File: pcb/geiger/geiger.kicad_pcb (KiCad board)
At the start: 2 copper layers, 160 x 112.4 mm, 125 parts, among them J1 Conn_01x02, J2 Conn_01x02, J3 Conn_01x03, J4 Conn_01x06, J5 Conn_01x02, J6 Conn_02x05_Odd_Even, J7 Conn_02x05_Odd_Even, K1 RELAY_DPST, Q1 BC140, Q2 BC107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

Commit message: Final version of geiger board.
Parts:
- moved R39 1.59 mm to (80.3, 82.2)
- moved C9 1.59 mm to (34.3, 27.6)
- moved R6 0.95 mm to (43.5, 27.3)
- moved D2 0.71 mm to (40.6, 34.0)
- moved C31 0.45 mm to (24.1, 54.9)
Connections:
- J4 pad 5: (no net) -> GND
- V1 pad 3: GND -> HEATER_6_3V
- V1 pad 4: HEATER_6_3V -> GND
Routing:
- net GND: track 98.3 -> 117.8 mm
- net HEATER_6_3V: track 66.8 -> 56.3 mm
- net HEATER1: track 101.7 -> 96.3 mm
- net Net-(Q6-Pad2): track 99.8 -> 102.4 mm
- net HEATER2: track 73.5 -> 71.6 mm
- net Net-(C24-Pad2): track 37.5 -> 35.9 mm
- net EYE_GRID: track 73.9 -> 75.5 mm
- net -VDC: track 140.1 -> 141.0 mm
- net +5V: track 268.1 -> 268.8 mm
- net Net-(D6-Pad1): track 70.4 -> 71.0 mm
- net Net-(C8-Pad1): track 58.8 -> 59.5 mm
- net Net-(D2-Pad1): track 4.49 -> 3.91 mm

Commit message: Change some element values geiger.
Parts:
- C33: value 10n -> 3n3
- Q4: value IRF540N -> AOT8N50
- R10: value 3k9 -> 4k7
- R11, R13, R14, R9: value 180k -> 470k
- R19: value 1M -> 1M6
- R31: value 100 -> 150
- R4: value 4k7 -> 2k2
- R42: value 100 -> 180
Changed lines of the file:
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@@
     (links 263)
     (no_connects 0)
-    (area 16.08 15.824999 194.936786 143.035001)
+    (area 16.142499 15.824999 176.262501 128.320001)
     (thickness 1.6)
     (drawings 11)
@@
   )
   (setup
-    (last_trace_width 0.8)
+    (last_trace_width 0.25)
     (user_trace_width 0.3)
     (user_trace_width 0.5)
@@
       (effects (font (size 1 1) (thickness 0.15)))
     )
-    (fp_text value 100 (at 5.08 2.31 180) (layer F.Fab)
+    (fp_text value 150 (at 5.08 2.31 180) (layer F.Fab)
       (effects (font (size 1 1) (thickness 0.15)))
     )
@@
       (effects (font (size 1 1) (thickness 0.15)))
     )
-    (fp_text value IRF540N (at 2.54 3.92) (layer F.Fab)
+    (fp_text value AOT8N50 (at 2.54 3.92) (layer F.Fab)
       (effects (font (size 1 1) (thickness 0.15)))
     )
@@
       (effects (font (size 1 1) (thickness 0.15)) (justify mirror))
     )
-    (fp_text value 180k (at 0 -1.9 270) (layer B.Fab)
+    (fp_text value 470k (at 0 -1.9 270) (layer B.Fab)
       (effects (font (size 1 1) (thickness 0.15)) (justify mirror))
     )
@@
       (effects (font (size 1 1) (thickness 0.15)) (justify mirror))
     )
-    (fp_text value 3k9 (at 0 -1.9 270) (layer B.Fab)
+    (fp_text value 4k7 (at 0 -1.9 270) (layer B.Fab)
       (effects (font (size 1 1) (thickness 0.15)) (justify mirror))
     )
@@
       (effects (font (size 1 1) (thickness 0.15)) (justify mirror))
     )
-    (fp_text value 180k (at 0 -1.9 270) (layer B.Fab)
+    (fp_text value 470k (at 0 -1.9 270) (layer B.Fab)
       (effects (font (size 1 1) (thickness 0.15)) (justify mirror))
     )
@@
       (effects (font (size 1 1) (thickness 0.15)) (justify mirror))
     )
-    (fp_text value 180k (at 0 -1.9 270) (layer B.Fab)
+    (fp_text value 470k (at 0 -1.9 270) (layer B.Fab)
       (effects (font (size 1 1) (thickness 0.15)) (justify mirror))
     )
@@
       (effects (font (size 1 1) (thickness 0.15)) (justify mirror))
     )
-    (fp_text value 180k (at 0 -1.9 270) (layer B.Fab)
+    (fp_text value 470k (at 0 -1.9 270) (layer B.Fab)
       (effects (font (size 1 1) (thickness 0.15)) (justify mirror))
     )
@@
       (effects (font (size 1 1) (thickness 0.15)))
     )
-    (fp_text value 4k7 (at 5.08 2.31 180) (layer F.Fab)
+    (fp_text value 2k2 (at 5.08 2.31 180) (layer F.Fab)
       (effects (font (size 1 1) (thickness 0.15)))
     )
@@
       (effects (font (size 1 1) (thickness 0.15)) (justify mirror))
     )
-    (fp_text value 10n (at 0 -2 270) (layer B.Fab)
+    (fp_text value 3n3 (at 0 -2 270) (layer B.Fab)
       (effects (font (size 1 1) (thickness 0.15)) (justify mirror))
     )
@@
       (effects (font (size 1 1) (thickness 0.15)))
     )
-    (fp_text value 1M (at 6.35 2.66 180) (layer F.Fab)
+    (fp_text value 1M6 (at 6.35 2.66 180) (layer F.Fab)
       (effects (font (size 1 1) (thickness 0.15)))
     )
@@
       (effects (font (size 1 1) (thickness 0.15)))
     )
-    (fp_text value 100 (at 7.62 2.66 90) (layer F.Fab)
+    (fp_text value 180 (at 7.62 2.66 90) (layer F.Fab)
       (effects (font (size 1 1) (thickness 0.15)))
     )

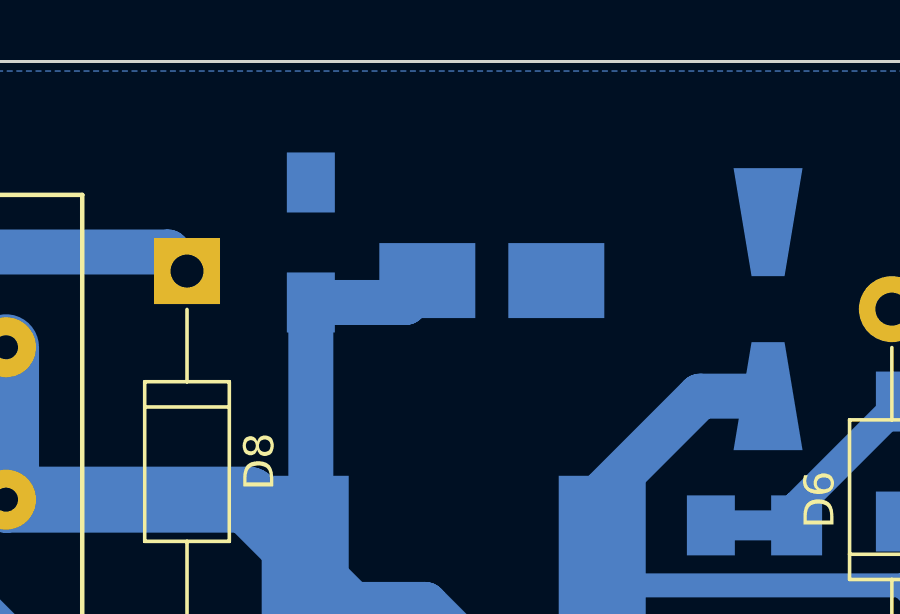
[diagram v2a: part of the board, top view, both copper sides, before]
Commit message: Update geiger element values.
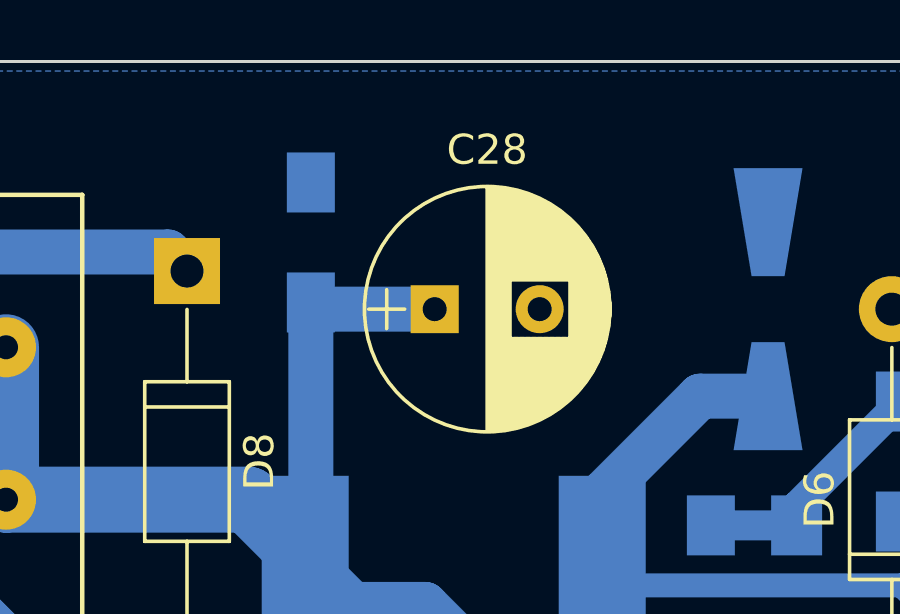
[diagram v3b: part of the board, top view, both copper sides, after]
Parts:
- C17: value 10n -> 3n3
- C28: value 22u -> 1000u; footprint Capacitors_Tantalum_SMD:CP_Tantalum_Case-B_EIA-3528-21_Hand -> Capacitors_ThroughHole:CP_Radial_D8.0mm_P3.50mm; moved to F.Cu
- C34: value 10n -> 6n8
- C35: value 33p -> 82p
- C39, C9: value 6u8 -> 4u7
- R1: value 1k -> 715
- R16: value 1k5 -> 1k
- R17: value 56k -> 68k
- R2: value 3k9 -> 2k2
- R20: value 475k -> 220k
- R3: value 3k9 -> 10k
- R39: value 6k8 -> 715
- R41: value 1R7 -> 22
- R5: value 3k9 -> 330
- R6: value 470 -> 68
- moved C28 2.13 mm to (126.0, 24.1)
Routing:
- net Net-(C17-Pad1): track 64.0 -> 63.0 mm

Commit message: Update element values on geiger board.
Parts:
- C35: value 82p -> 180p
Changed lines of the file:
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@@
       (effects (font (size 1 1) (thickness 0.15)))
     )
-    (fp_text value 82p (at 3.75 2.91) (layer F.Fab)
+    (fp_text value 180p (at 3.75 2.91) (layer F.Fab)
       (effects (font (size 1 1) (thickness 0.15)))
     )

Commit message: Update all Kicad files to Kicad 5.
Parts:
- R35: value 10k -> 4k7
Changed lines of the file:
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@@
-(kicad_pcb (version 4) (host pcbnew 4.0.7)
+(kicad_pcb (version 20171130) (host pcbnew 5.0.1)
   (general
-    (links 263)
-    (no_connects 0)
-    (area 16.142499 15.824999 176.262501 128.320001)
     (thickness 1.6)
     (drawings 11)
@@
     (pad_drill 0.8)
     (pad_to_mask_clearance 0)
+    (solder_mask_min_width 0.25)
     (aux_axis_origin 0 0)
     (grid_origin 127.3175 161.29)
@@
       (layerselection 0x00000_80000000)
       (usegerberextensions false)
+      (usegerberattributes false)
+      (usegerberadvancedattributes false)
+      (creategerberjobfile false)
       (excludeedgelayer false)
       (linewidth 0.100000)
@@
       (hpglpennumber 1)
       (hpglpenspeed 20)
-      (hpglpendiameter 15)
-      (hpglpenoverlay 2)
+      (hpglpendiameter 15.000000)
       (psnegative false)
       (psa4output false)
@@
       (drillshape 2)
       (scaleselection 1)
-      (outputdirectory ./))
+      (outputdirectory "./"))
   )
   (net 0 "")
@@
       (net 61 "Net-(J1-Pad1)"))
     (model Terminal_Blocks.3dshapes/TerminalBlock_Pheonix_MKDS1.5-2pol.wrl
-      (at (xyz 0.0984 0 0))
+      (offset (xyz 2.499359962463379 0 0))
       (scale (xyz 1 1 1))
       (rotate (xyz 0 0 0))
@@
       (net 9 "Net-(C22-Pad1)"))
     (model ${KISYS3DMOD}/TO_SOT_Packages_THT.3dshapes/TO-92_Molded_Wide.wrl
-      (at (xyz 0.1 0 0))
+      (offset (xyz 2.539999961853027 0 0))
       (scale (xyz 1 1 1))
       (rotate (xyz 0 0 -90))
@@
       (net 55 +36V))
     (model Terminal_Blocks.3dshapes/TerminalBlock_Pheonix_MKDS1.5-2pol.wrl
-      (at (xyz 0.0984 0 0))
+      (offset (xyz 2.499359962463379 0 0))
       (scale (xyz 1 1 1))
       (rotate (xyz 0 0 0))
@@
       (net 2 GND))
     (model Terminal_Blocks.3dshapes/TerminalBlock_Pheonix_MKDS1.5-2pol.wrl
-      (at (xyz 0.0984 0 0))
+      (offset (xyz 2.499359962463379 0 0))
       (scale (xyz 1 1 1))
       (rotate (xyz 0 0 0))
@@
       (net 2 GND))
     (model ${KISYS3DMOD}/TO_SOT_Packages_THT.3dshapes/TO-220-3_Vertical.wrl
-      (at (xyz 0.1 0 0))
+      (offset (xyz 2.539999961853027 0 0))
       (scale (xyz 0.393701 0.393701 0.393701))
       (rotate (xyz 0 0 0))
@@
       (effects (font (size 1 1) (thickness 0.15)) (justify mirror))
     )
-    (fp_text user %R (at 0 0 360) (layer B.Fab)
+    (fp_text user %R (at 0 0) (layer B.Fab)
       (effects (font (size 0.5 0.5) (thickness 0.075)) (justify mirror))
     )
@@
       (effects (font (size 1 1) (thickness 0.15)) (justify mirror))
     )
-    (fp_text value 10k (at 0 -1.9 90) (layer B.Fab)
+    (fp_text value 4k7 (at 0 -1.9 90) (layer B.Fab)
       (effects (font (size 1 1) (thickness 0.15)) (justify mirror))
     )
@@
       (net 2 GND))
     (model ${KISYS3DMOD}/TO_SOT_Packages_THT.3dshapes/TO-220-3_Vertical.wrl
-      (at (xyz 0.1 0 0))
+      (offset (xyz 2.539999961853027 0 0))
       (scale (xyz 0.393701 0.393701 0.393701))
       (rotate (xyz 0 0 0))
@@
       (effects (font (size 1 1) (thickness 0.15)) (justify mirror))
     )
-    (fp_text user %R (at 0 0 450) (layer B.Fab)
+    (fp_text user %R (at 0 0 90) (layer B.Fab)
       (effects (font (size 0.5 0.5) (thickness 0.075)) (justify mirror))
     )

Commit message: Update values on PCB.
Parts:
- C8: value 100n -> 1u
- R15: value 1M6 -> 470k
- R20: value 220k -> 470k
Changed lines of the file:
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@@
       (effects (font (size 1 1) (thickness 0.15)))
     )
-    (fp_text value 100n (at 13.75 7.81 270) (layer F.Fab)
+    (fp_text value 1u (at 13.75 7.81 270) (layer F.Fab)
       (effects (font (size 1 1) (thickness 0.15)))
     )
@@
       (effects (font (size 1 1) (thickness 0.15)) (justify mirror))
     )
-    (fp_text value 220k (at 0 -1.9 90) (layer B.Fab)
+    (fp_text value 470k (at 0 -1.9 90) (layer B.Fab)
       (effects (font (size 1 1) (thickness 0.15)) (justify mirror))
     )
@@
       (effects (font (size 1 1) (thickness 0.15)))
     )
-    (fp_text value 1M6 (at 6.35 2.66 180) (layer F.Fab)
-      (effects (font (size 1 1) (thickness 0.15)))
-    )
+    (fp_text value 470k (at 6.35 2.66 180) (layer F.Fab)
+      (effects (font (size 1 1) (thickness 0.15)))
+    )

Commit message: Migrate to KiCAD 9.
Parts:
- C11: value 2u2 -> 10u
- C8: value 1u -> 2u2
- Q6: value IRF540N -> IRF740A
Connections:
- J6 pad 4: (no net) -> unconnected-(J6-Pin_4-Pad4)
- J6 pad 6: (no net) -> unconnected-(J6-Pin_6-Pad6)
- J6 pad 7: (no net) -> unconnected-(J6-Pin_7-Pad7)
- J7 pad 4: (no net) -> unconnected-(J7-Pin_4-Pad4)
- J7 pad 6: (no net) -> unconnected-(J7-Pin_6-Pad6)
- J7 pad 7: (no net) -> unconnected-(J7-Pin_7-Pad7)
- U1 pad 18: (no net) -> unconnected-(U1-XOUT/P2.7-Pad18)
- U1 pad 2: (no net) -> unconnected-(U1-P1.0/TA0CLK/ACLK/A0/CA0-Pad2)
- U1 pad 8: (no net) -> unconnected-(U1-P2.0/TA1.0-Pad8)
- U2 pad 9: (no net) -> unconnected-(U2-~{QH}-Pad9)
- U4 pad 1: (no net) -> unconnected-(U4-C1-Pad1)
- U4 pad 8: (no net) -> unconnected-(U4-C2-Pad8)
- V1 pad 6: (no net) -> unconnected-(V1-Pad6)
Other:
- net class Default removed
